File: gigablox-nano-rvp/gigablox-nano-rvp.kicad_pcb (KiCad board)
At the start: 2 copper layers, 23 parts, among them IC1 MAX6898AAZT+T, J1 Conn_01x02, J2 Conn_01x03, J3 Conn_01x04, J4 Conn_01x02, Q1 Q_PMOS_GSD, U1 LM4040DIM3-3.0

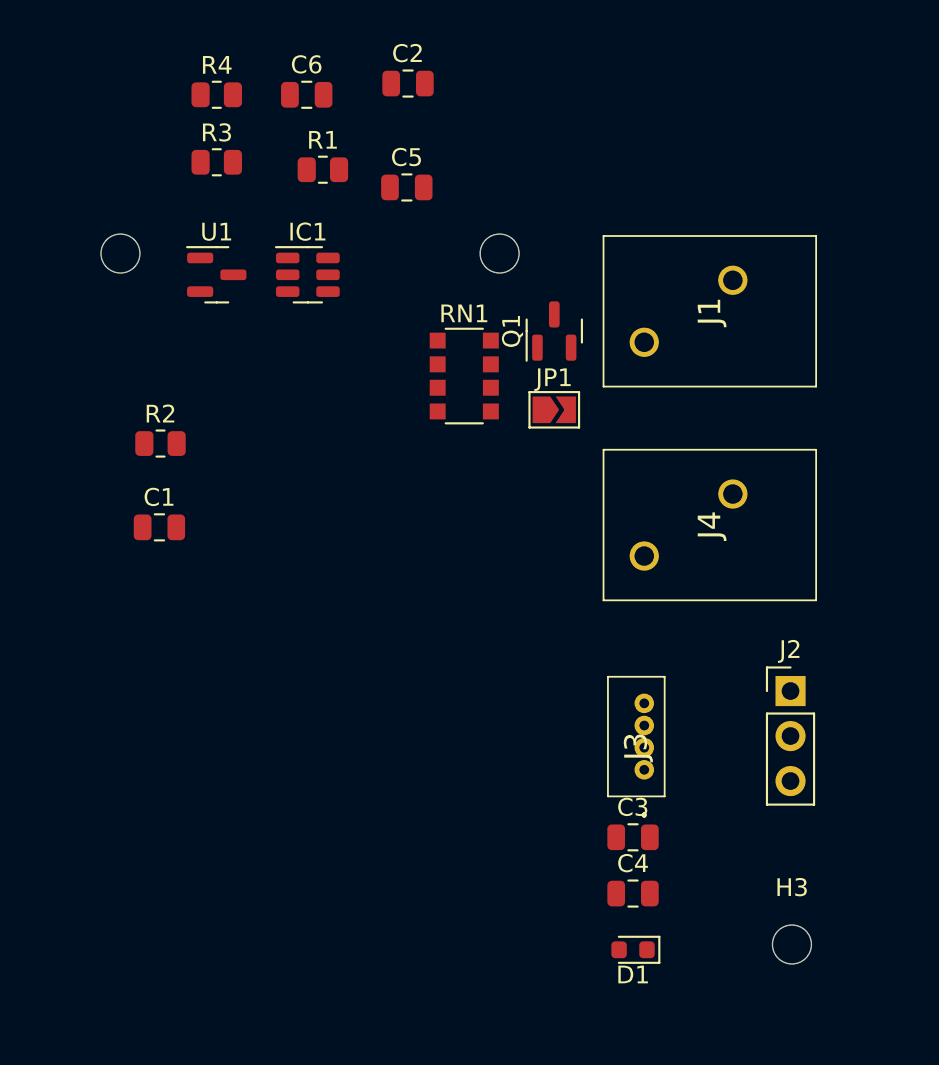
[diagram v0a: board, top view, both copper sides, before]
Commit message: new jetson-nano-ppoe and gigablox-nano-rvp gerbers
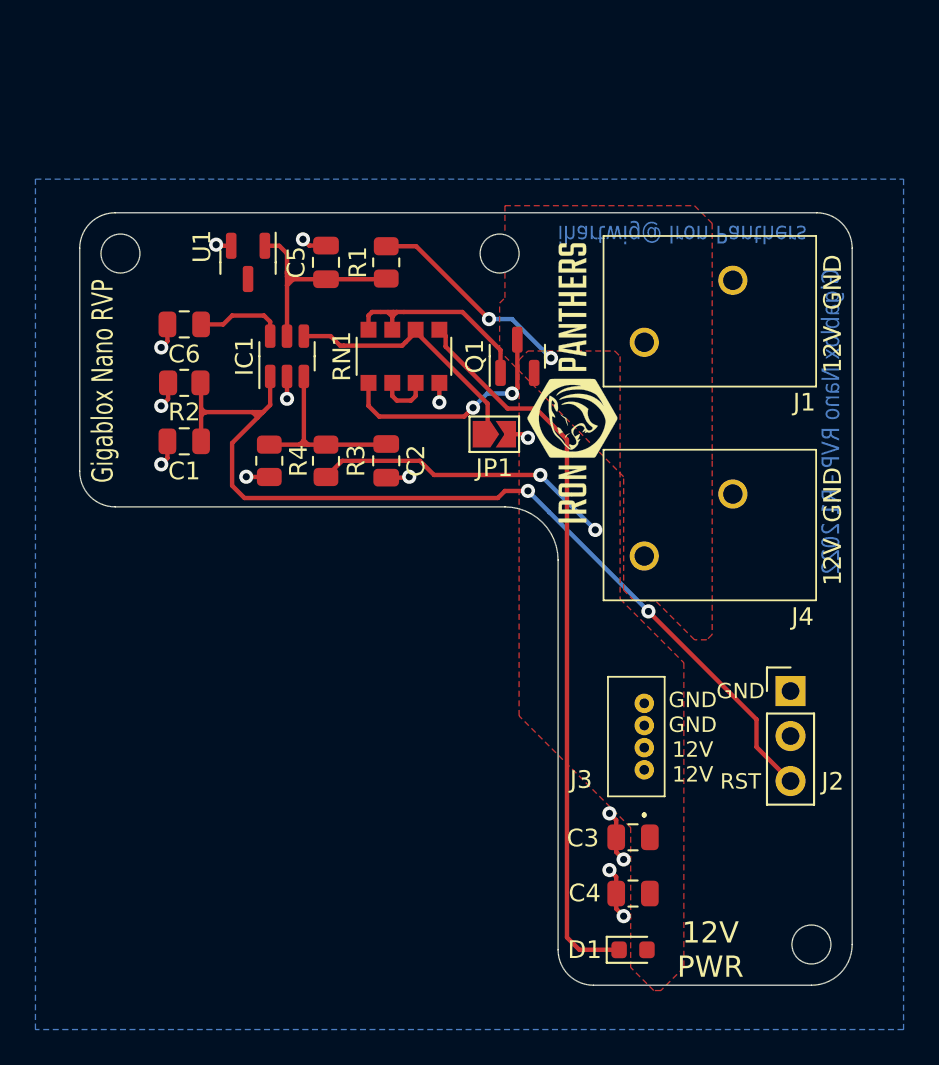
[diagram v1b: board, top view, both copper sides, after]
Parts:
- added G***: LOGO, frc-on-ftc-hw:iron_panthers_wordmark_silk_5mm, F.Cu at (122.3, 31.5)
- moved C2 21.3 mm to (111.8, 35.9), turned to -90 degrees
- moved R4 20.9 mm to (105.2, 35.9), turned to -90 degrees
- moved R3 17.9 mm to (108.4, 35.9), turned to 90 degrees
- moved C6 14.7 mm to (100.4, 28.2), turned to 180 degrees
- moved R1 6.34 mm to (111.8, 24.7), turned to -90 degrees
- moved C5 6.22 mm to (108.4, 24.7), turned to 90 degrees
- moved C1 5.05 mm to (100.4, 34.8), turned to 180 degrees
- moved IC1 4.75 mm to (106.2, 30.0), turned to 90 degrees
- moved R2 3.68 mm to (100.4, 31.5), turned to 180 degrees
- moved JP1 3.66 mm to (117.9, 34.4)
- moved RN1 3.58 mm to (112.8, 30.0), turned to 90 degrees
- moved Q1 2.53 mm to (119.2, 30.0)
- moved U1 1.90 mm to (104.0, 24.7), turned to -90 degrees
- moved H3 1.10 mm to (135.8, 63.2)
- turned C3 to 180 degrees
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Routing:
- net /RST_CONN: track 0.00 -> 54.6 mm, vias 0 -> 2
- net /REG_VIN_K: track 0.00 -> 41.5 mm
- net +12V: track 0.00 -> 29.1 mm, vias 0 -> 4
- net GND: track 0.00 -> 18.8 mm, vias 0 -> 14
- net /12V_CONN_EN: track 0.00 -> 14.7 mm
- net /12V_CONN: track 0.00 -> 13.3 mm, vias 0 -> 2
- net +3V0: track 0.00 -> 12.8 mm
- net /12V_CONN_R: track 0.00 -> 12.3 mm
- net /RST_IN: track 0.00 -> 10.9 mm
- net /RST_CDELAY: track 0.00 -> 5.06 mm
- net Net-(RN1-Pad2): track 0.00 -> 3.02 mm
- added copper zone on F.Cu, net +12V
- added copper zone on F.Cu, net /12V_CONN
- added copper zone on B.Cu, net GND
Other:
- board outline added: 43.6 x 43.6 mm
- board text added: "12V GND"
- board text added: "12V PWR"
- board text added: "GND"
- board text added: "GND GND 12V 12V"
- board text added: "Gigablox Nano RVP"
- board text added: "Gigablox Nano RVP - R1 2022"
- board text added: "RST"
- board text added: "ihartwig@ Iron Panthers"

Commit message: gigablox-nano-rvp and jetson-nano-ppoe gerbers
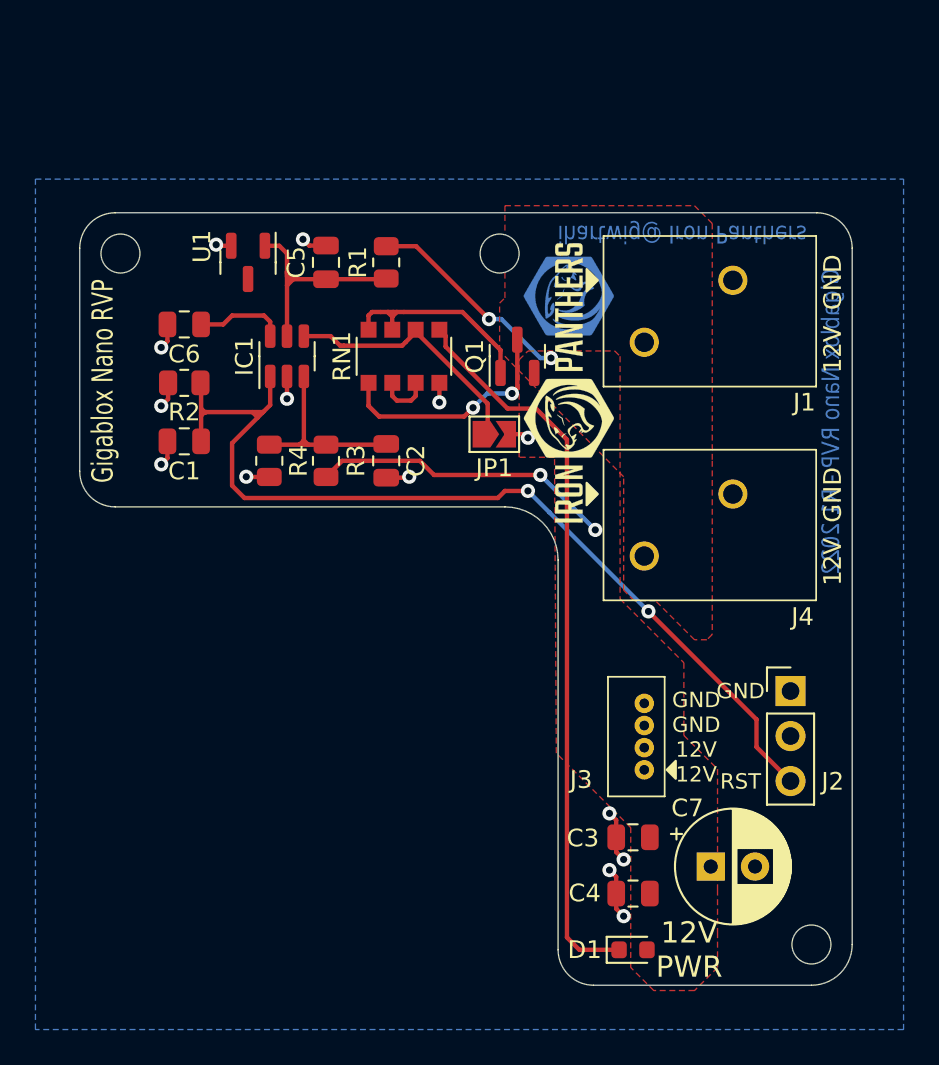
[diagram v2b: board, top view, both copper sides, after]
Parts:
- added C7: DNP, Capacitor_THT:CP_Radial_D6.3mm_P2.50mm, F.Cu at (130.1, 58.8)
- added G***: LOGO, frc-on-ftc-hw:iron_panthers_logo_fcu_5mm, B.Cu at (122.1, 26.6)
- moved G*** 0.20 mm to (122.1, 31.5)
